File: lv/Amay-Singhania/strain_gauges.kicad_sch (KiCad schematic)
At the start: 6 parts, among them U2 AD8222HACPZ-R7, U3 AD8222HACPZ-R7, U4 AD8222HACPZ-R7, U5 AD8222HACPZ-R7, U6 AD8222HACPZ-R7, U7 AD8222HACPZ-R7

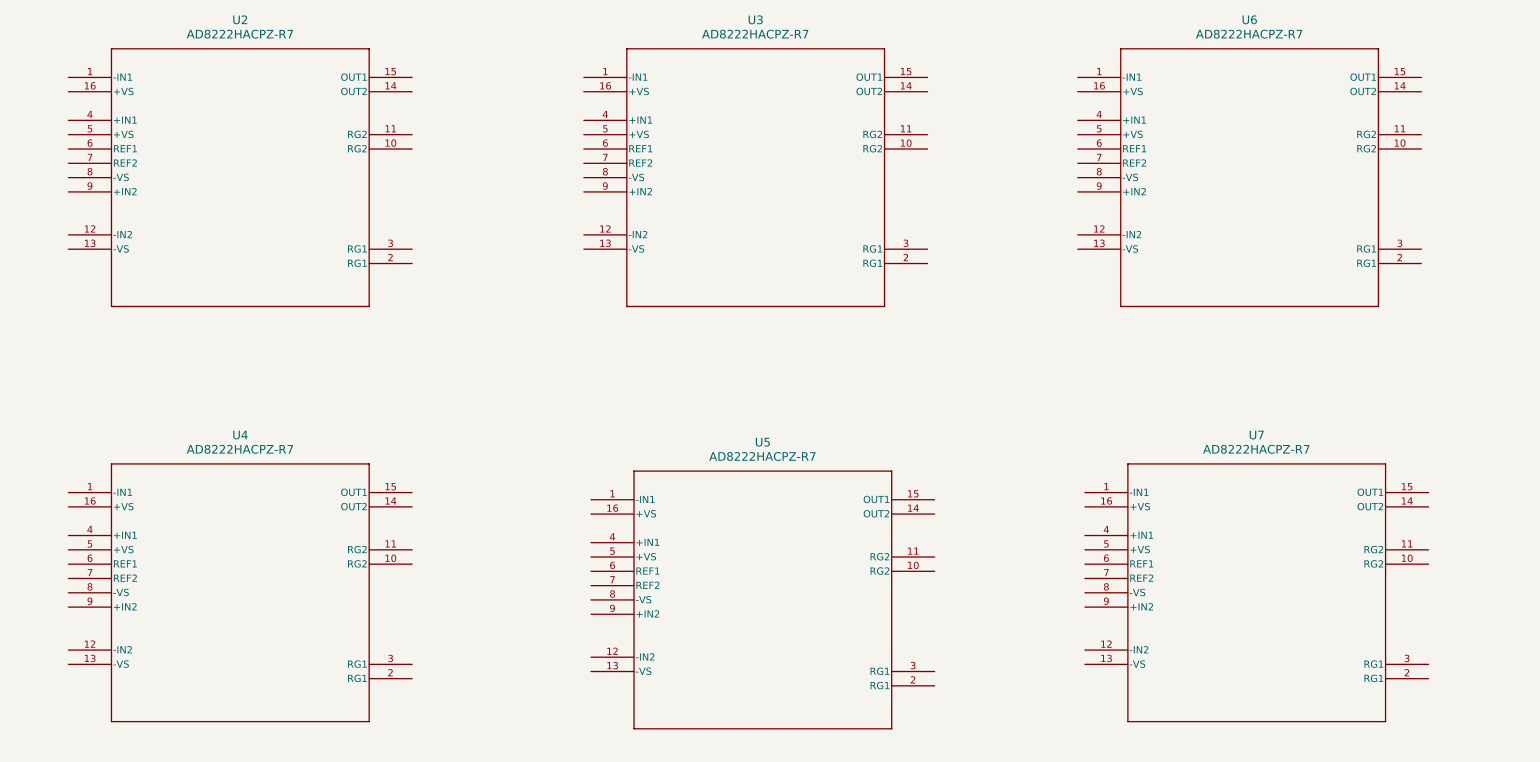
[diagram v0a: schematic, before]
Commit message: wired instrumentation amps and calculated gain measurements
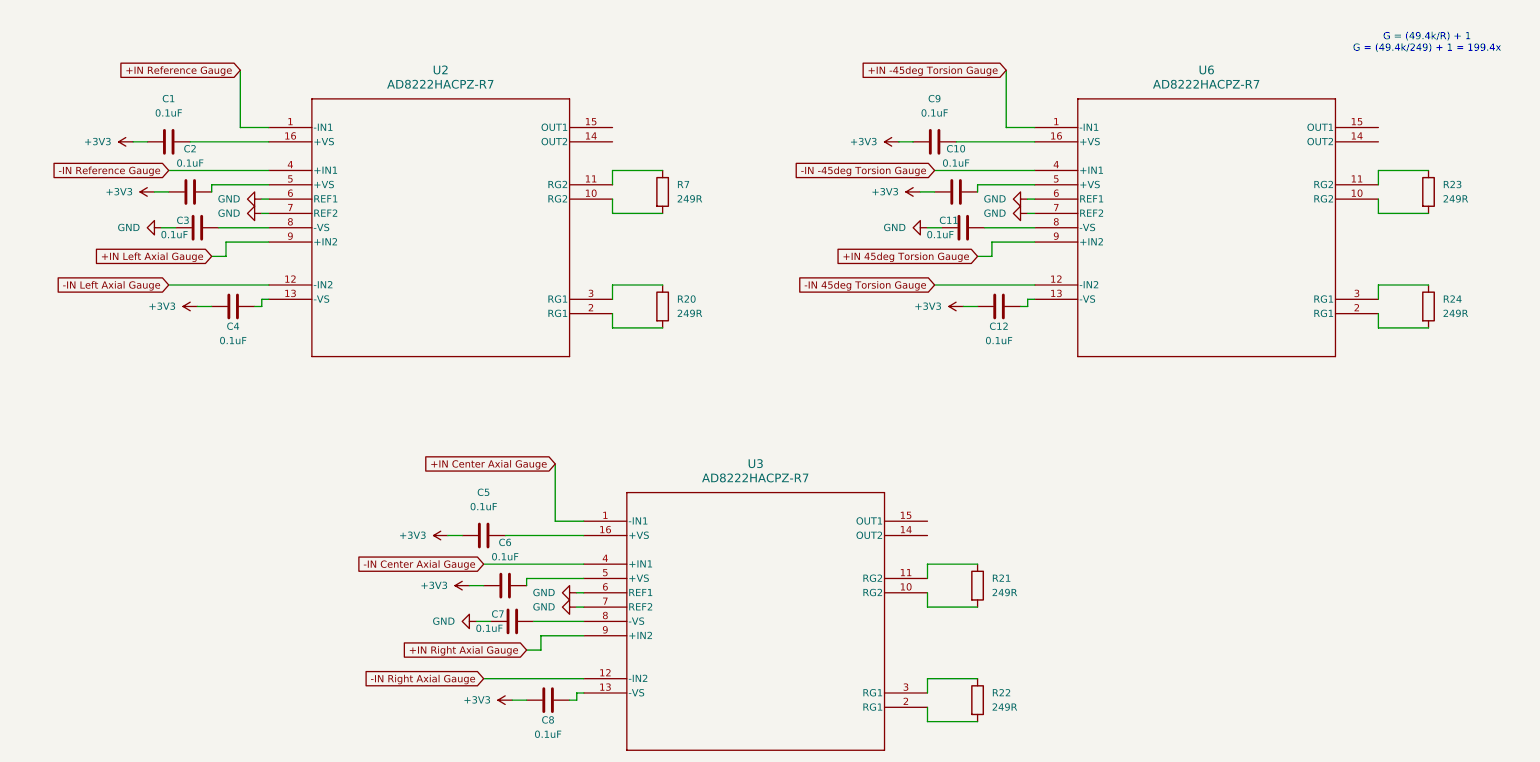
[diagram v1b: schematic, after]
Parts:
- removed U4, U5, U7: AD8222HACPZ-R7, AD8222:CP_16_19_ADI, symbol AD8222:AD8222HACPZ-R7
- added C1, C10, C11, C12, C2, C3, C4, C5, C6, C7, C8, C9: 0.1uF, Package_TO_SOT_SMD:TSOT-23-5, symbol Device:C
- added R20, R21, R22, R23, R24, R7: 249R, Package_DIP:DIP-8_W7.62mm, symbol Device:R
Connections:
- net +IN Reference Gauge: now reaches U2.1 (-IN1)
- net at U2.10 (RG2): now also R7.2
- net at U2.11 (RG2): now also R7.1
- net -IN Left Axial Gauge: now reaches U2.12 (-IN2)
- net at U2.13 (-VS): now also C4.2
- net at U2.16 (+VS): now also C1.2
- net at U2.2 (RG1): now also R20.2
- net at U2.3 (RG1): now also R20.1
- net -IN Reference Gauge: now reaches U2.4 (+IN1)
- net at U2.5 (+VS): now also C2.2
- net GND: now reaches U2.6 (REF1)
- net GND: now also U2.7 (REF2), U3.6 (REF1), U3.7 (REF2), U6.6 (REF1), U6.7 (REF2), C11.1, C3.1, C7.1
- net at U2.8 (-VS): now also C3.2
- net +IN Left Axial Gauge: now reaches U2.9 (+IN2)
- net +IN -45deg Torsion Gauge: now reaches U6.1 (-IN1)
- net at U6.10 (RG2): now also R23.2
- net at U6.11 (RG2): now also R23.1
- net -IN 45deg Torsion Gauge: now reaches U6.12 (-IN2)
- net at U6.13 (-VS): now also C12.2
- net at U6.16 (+VS): now also C9.2
- net at U6.2 (RG1): now also R24.2
- net at U6.3 (RG1): now also R24.1
- net -IN -45deg Torsion Gauge: now reaches U6.4 (+IN1)
- net at U6.5 (+VS): now also C10.2
- net at U6.8 (-VS): now also C11.2
- net +IN 45deg Torsion Gauge: now reaches U6.9 (+IN2)
- net +IN Center Axial Gauge: now reaches U3.1 (-IN1)
- net at U3.10 (RG2): now also R21.2
- net at U3.11 (RG2): now also R21.1
- net -IN Right Axial Gauge: now reaches U3.12 (-IN2)
- net at U3.13 (-VS): now also C8.2
- net at U3.16 (+VS): now also C5.2
- net at U3.2 (RG1): now also R22.2
- net at U3.3 (RG1): now also R22.1
- net -IN Center Axial Gauge: now reaches U3.4 (+IN1)
- net at U3.5 (+VS): now also C6.2
- net at U3.8 (-VS): now also C7.2
- net +IN Right Axial Gauge: now reaches U3.9 (+IN2)
- new net +3V3: C1.1, C10.1, C12.1, C2.1, C4.1, C5.1, C6.1, C8.1, C9.1
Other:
- note added: "G = (49.4k/R) + 1 G = (49.4k/249) + 1 = 199.4x"
- moved on the sheet: U2, U3, U6
